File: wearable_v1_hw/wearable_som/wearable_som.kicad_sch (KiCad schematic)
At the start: 6 parts, among them SW1 Reset, U1 STM32WB55RGVx, Y1 Crystal_GND23

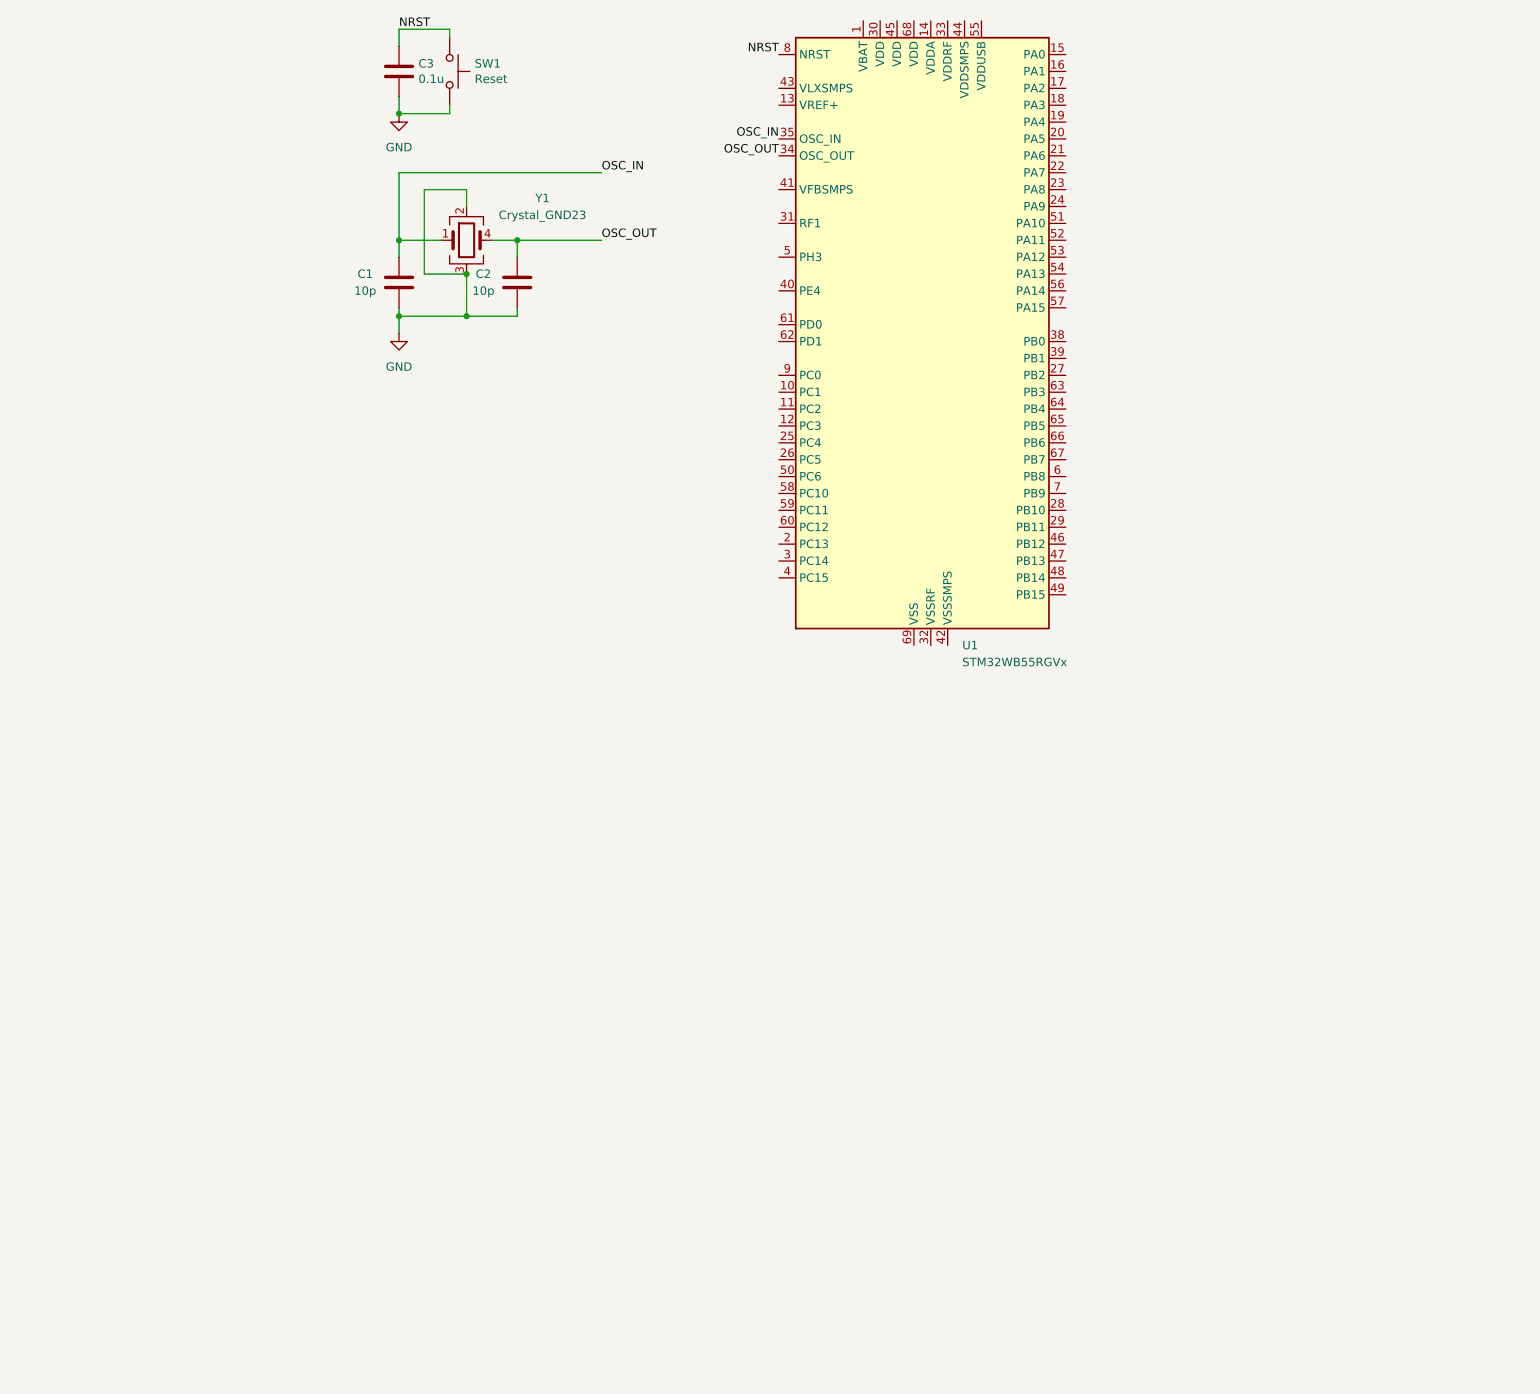
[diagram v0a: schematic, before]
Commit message: done with power circuitry
uses mcp73831 and ldo for lipo charging
(^._.^)ﾉ😜
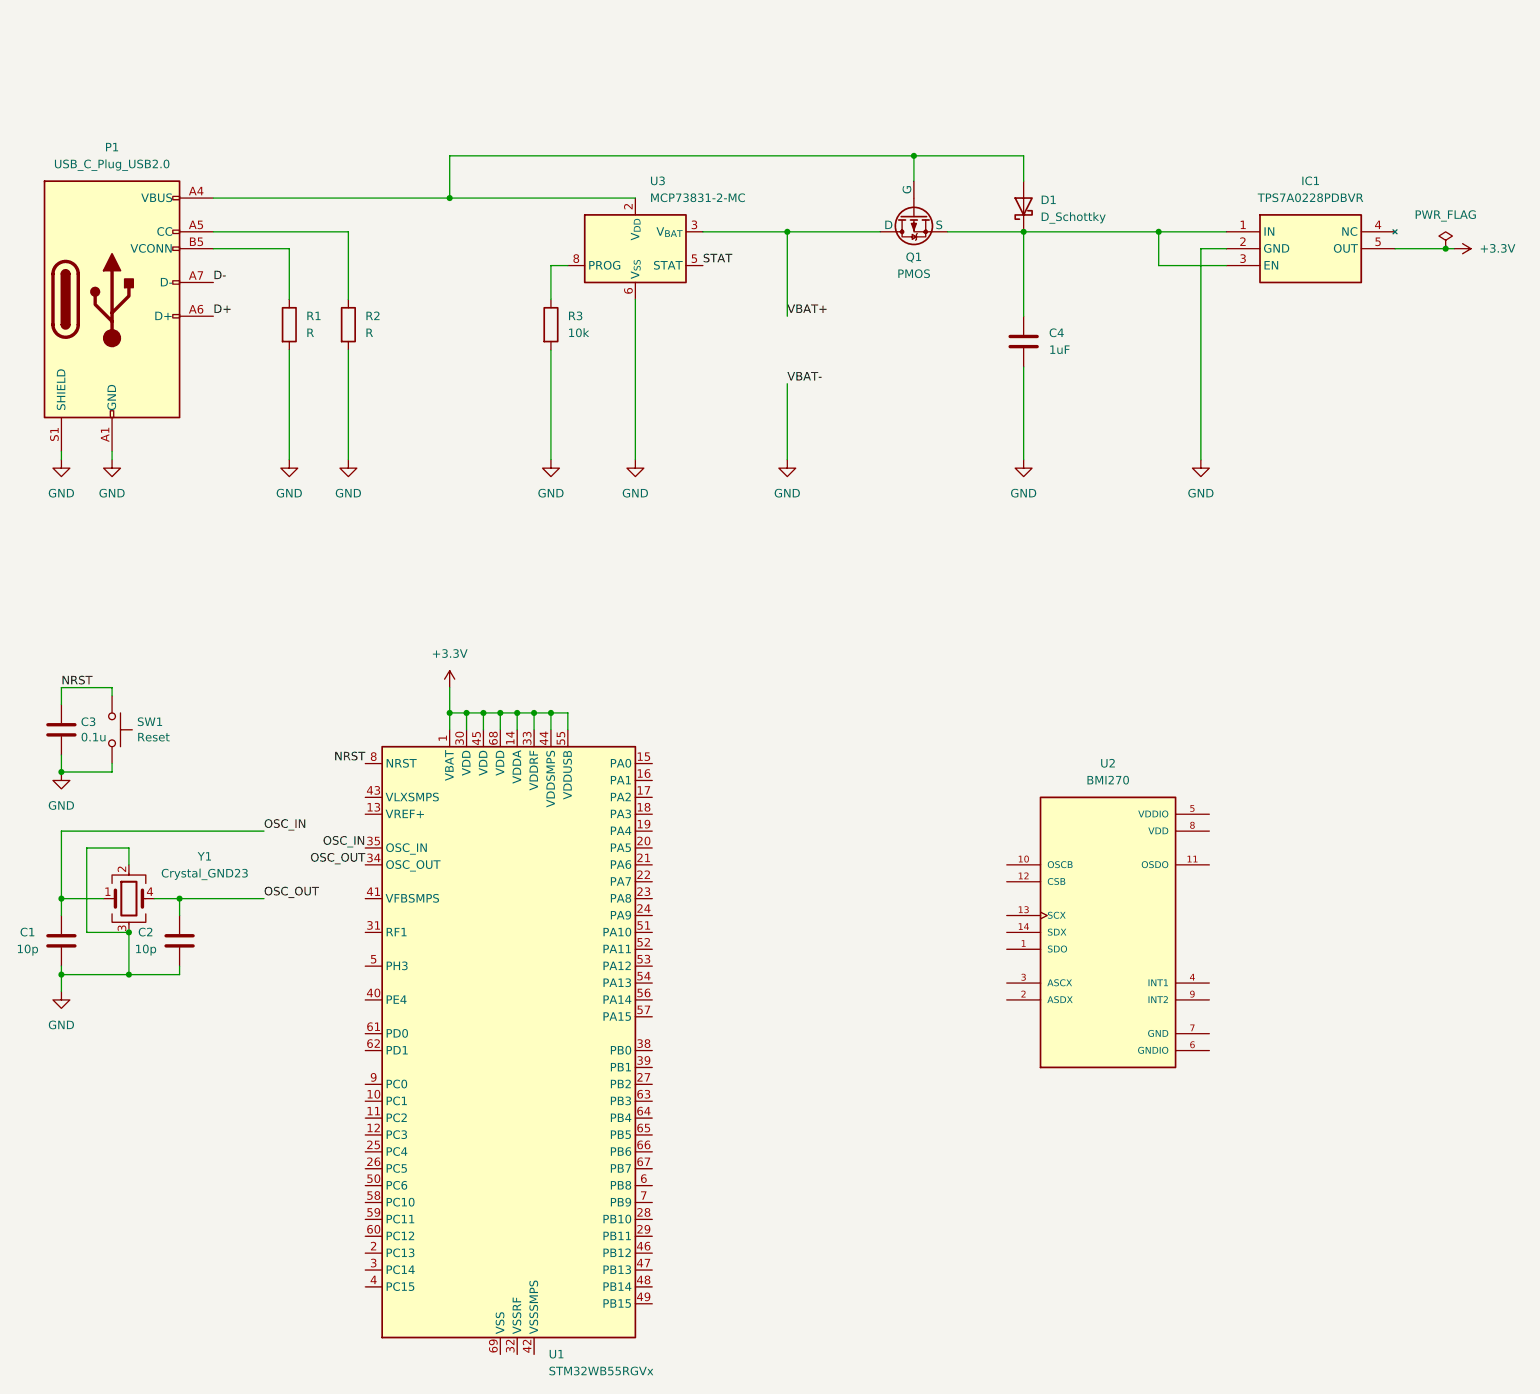
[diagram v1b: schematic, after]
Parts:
- added C4: 1uF, symbol Device:C
- added D1: D_Schottky, wearable_som_footprint_lib:SOD2513X120N, symbol Device:D_Schottky
- added IC1: TPS7A0228PDBVR, wearable_som_footprint_lib:SOT95P280X145-5N, symbol wearable-som-sym-lib:TPS7A0228PDBVR
- added P1: USB_C_Plug_USB2.0, symbol Connector:USB_C_Plug_USB2.0
- added Q1: PMOS, wearable_som_footprint_lib:SOT96P240X110-3N, symbol Simulation_SPICE:PMOS
- added R1, R2: R, symbol Device:R
- added R3: 10k, symbol Device:R
- added U2: BMI270, BMI270:XDCR_BMI270, symbol BMI270:BMI270
- added U3: MCP73831-2-MC, Package_DFN_QFN:DFN-8-1EP_3x2mm_P0.5mm_EP1.7x1.4mm, symbol Battery_Management:MCP73831-2-MC
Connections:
- net GND: now also C4.2, IC1.2 (GND), P1.A1 (GND), P1.A12 (GND), P1.B1 (GND), P1.B12 (GND), P1.S1 (SHIELD), R1.2, R2.2, R3.2, U3.6 (V_{SS})
- net +3.3V: now reaches U1.1 (VBAT)
- net +3.3V: now also U1.14 (VDDA), U1.30 (VDD), U1.33 (VDDRF), U1.44 (VDDSMPS), U1.45 (VDD), U1.55 (VDDUSB), U1.68 (VDD), IC1.5 (OUT)
- new net: D1.2 (A), P1.A4 (VBUS), P1.A9 (VBUS), P1.B4 (VBUS), P1.B9 (VBUS), Q1.2 (G), U3.1 (V_{DD}), U3.2 (V_{DD})
- new net: C4.1, D1.1 (K), IC1.1 (IN), IC1.3 (EN), Q1.3 (S)
- new net: P1.A5 (CC), R2.1
- new net: P1.B5 (VCONN), R1.1
- new net: R3.1, U3.8 (PROG)
- new net D+: P1.A6 (D+)
- new net D-: P1.A7 (D-)
- new net STAT: U3.5 (STAT)
- new net VBAT+: Q1.1 (D), U3.3 (V_{BAT}), U3.4 (V_{BAT})
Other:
- moved on the sheet: C1, C2, C3, SW1, U1, Y1

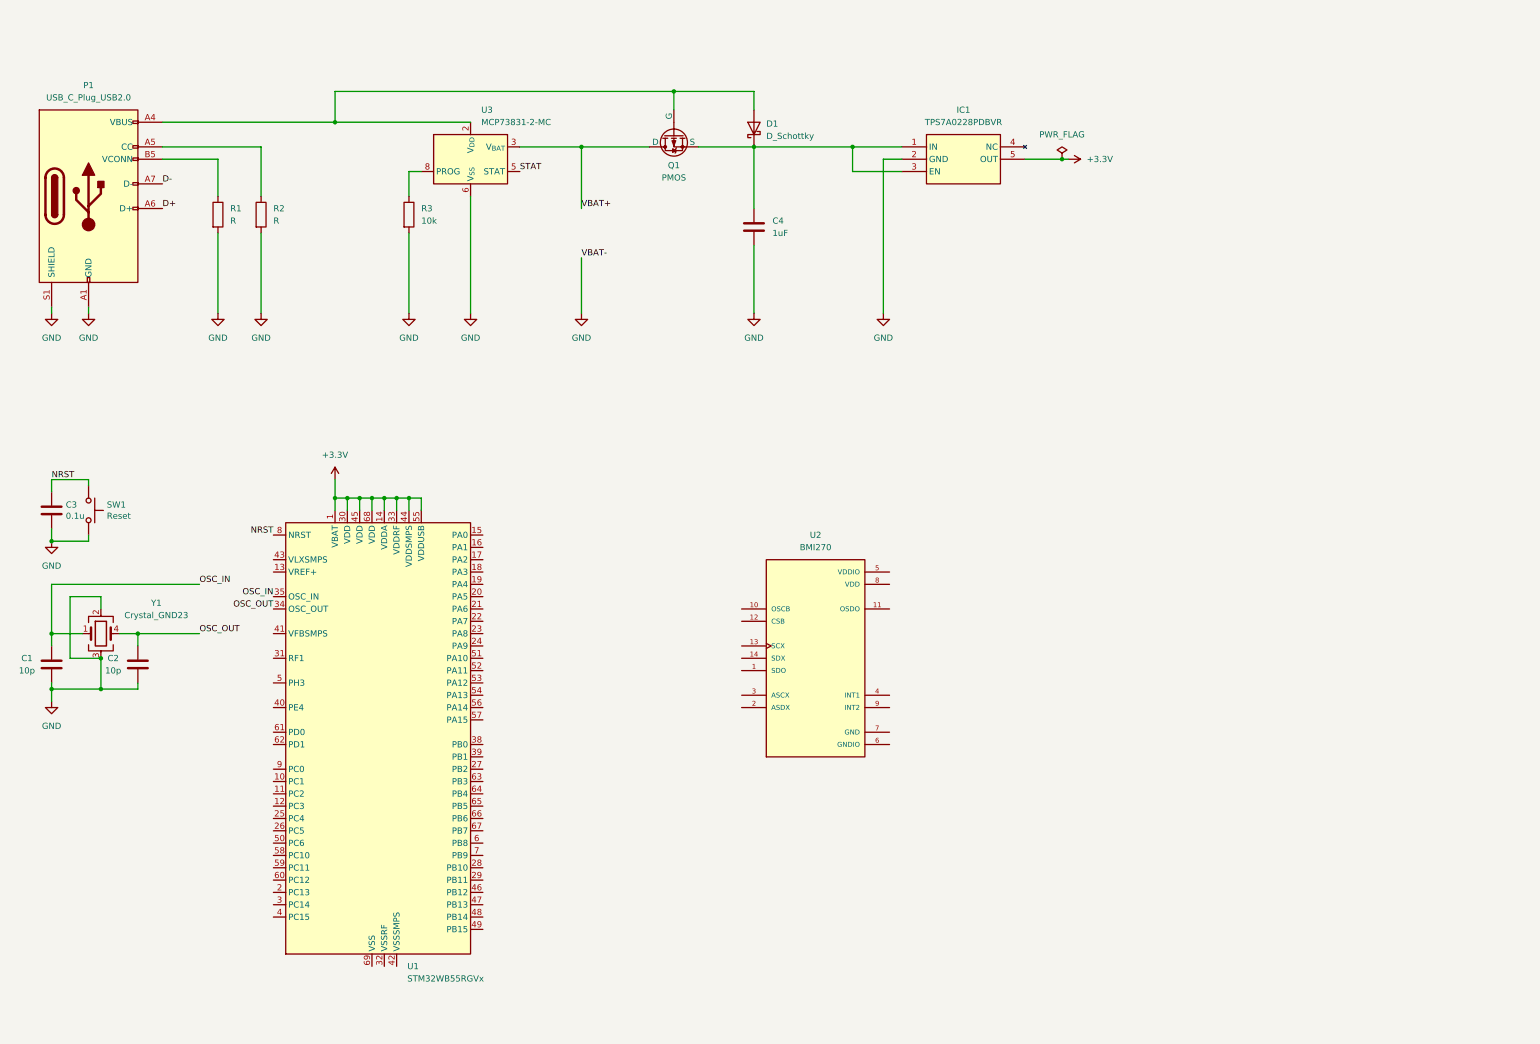
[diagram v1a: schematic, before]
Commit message: added imu, rf circuitry📡😹
💃
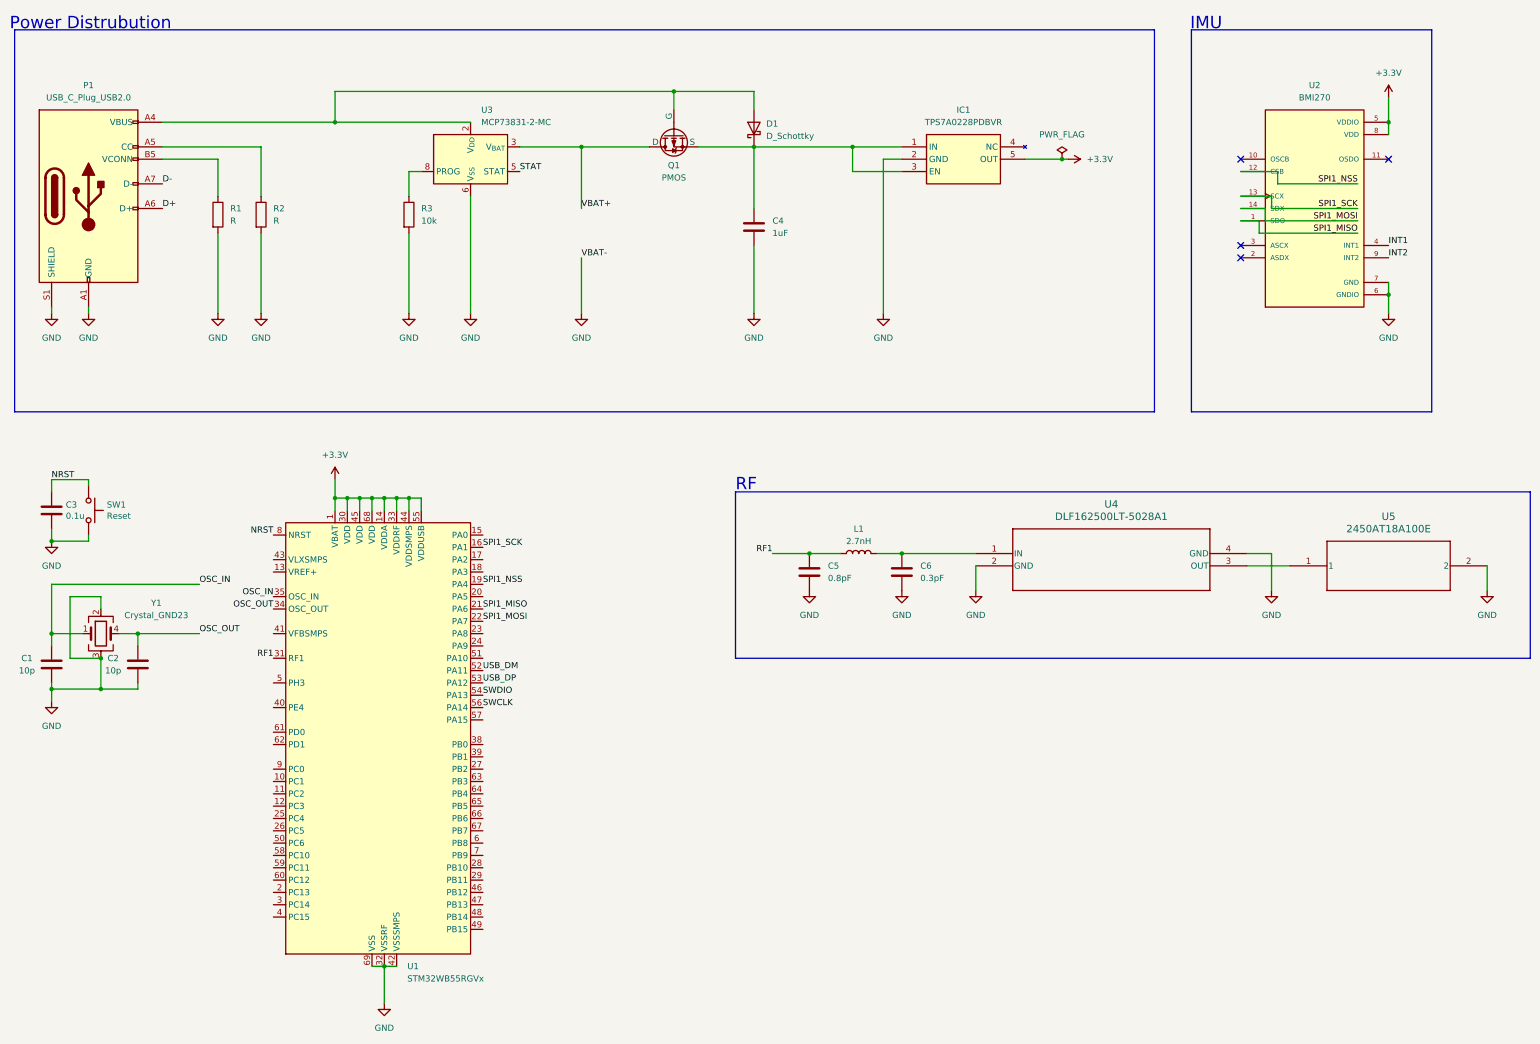
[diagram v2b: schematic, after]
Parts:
- added C5: 0.8pF, symbol Device:C
- added C6: 0.3pF, symbol Device:C
- added L1: 2.7nH, symbol Device:L
- added U4: DLF162500LT-5028A1, DLF-4_1P6X0P8, symbol wearable-som-sym-lib:DLF162500LT-5028A1
- added U5: 2450AT18A100E, 2450AT18A100E_JOT, symbol wearable-som-sym-lib:2450AT18A100E
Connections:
- net +3.3V: now also U2.5 (VDDIO), U2.8 (VDD)
- net GND: now also U1.32 (VSSRF), U1.42 (VSSSMPS), U1.69 (VSS), U2.6 (GNDIO), U2.7 (GND), C5.2, C6.2, U4.2 (GND), U4.4 (GND), U5.2
- net SPI1_SCK: now reaches U1.16 (PA1)
- net SPI1_SCK: now also U2.13 (SCX)
- net SPI1_NSS: now reaches U1.19 (PA4)
- net SPI1_NSS: now also U2.12 (CSB)
- net SPI1_MISO: now reaches U1.21 (PA6)
- net SPI1_MISO: now also U2.1 (SDO)
- net SPI1_MOSI: now reaches U1.22 (PA7)
- net SPI1_MOSI: now also U2.14 (SDX)
- net RF1: now reaches U1.31 (RF1)
- net RF1: now also C5.1, L1.1
- net USB_DM: now reaches U1.52 (PA11)
- net USB_DP: now reaches U1.53 (PA12)
- net SWDIO: now reaches U1.54 (PA13)
- net SWCLK: now reaches U1.56 (PA14)
- net INT1: now reaches U2.4 (INT1)
- net INT2: now reaches U2.9 (INT2)
- new net: U4.3 (OUT), U5.1
- new net: C6.1, L1.2, U4.1 (IN)
- no-connect marks 0 -> 4
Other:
- note added: "IMU"
- note added: "Power Distrubution"
- note added: "RF"
- moved on the sheet: U2
